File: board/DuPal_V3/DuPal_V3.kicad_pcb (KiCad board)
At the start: 2 copper layers, 116.8 x 73.7 mm, 132 parts, among them J1 ZIF Socket, J2 Debug Header, J3 Extra, J4 Conn_01x21_Pin, J5 Conn_01x21_Pin, K1 G6K-2, Q1 2N3904, SW1 RESET, U1 Pico, U10 74HCT166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

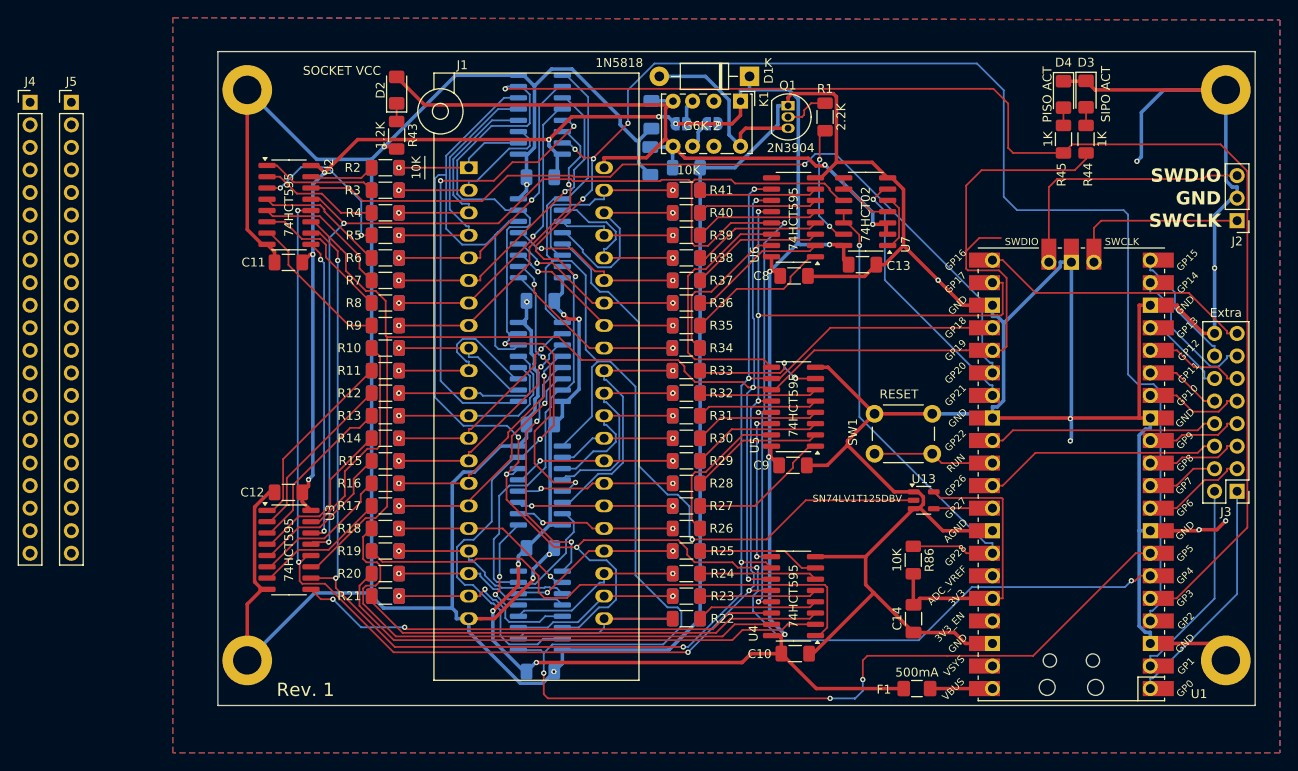
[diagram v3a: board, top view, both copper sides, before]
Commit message: Add pinheaders to rev. 1 V3 board
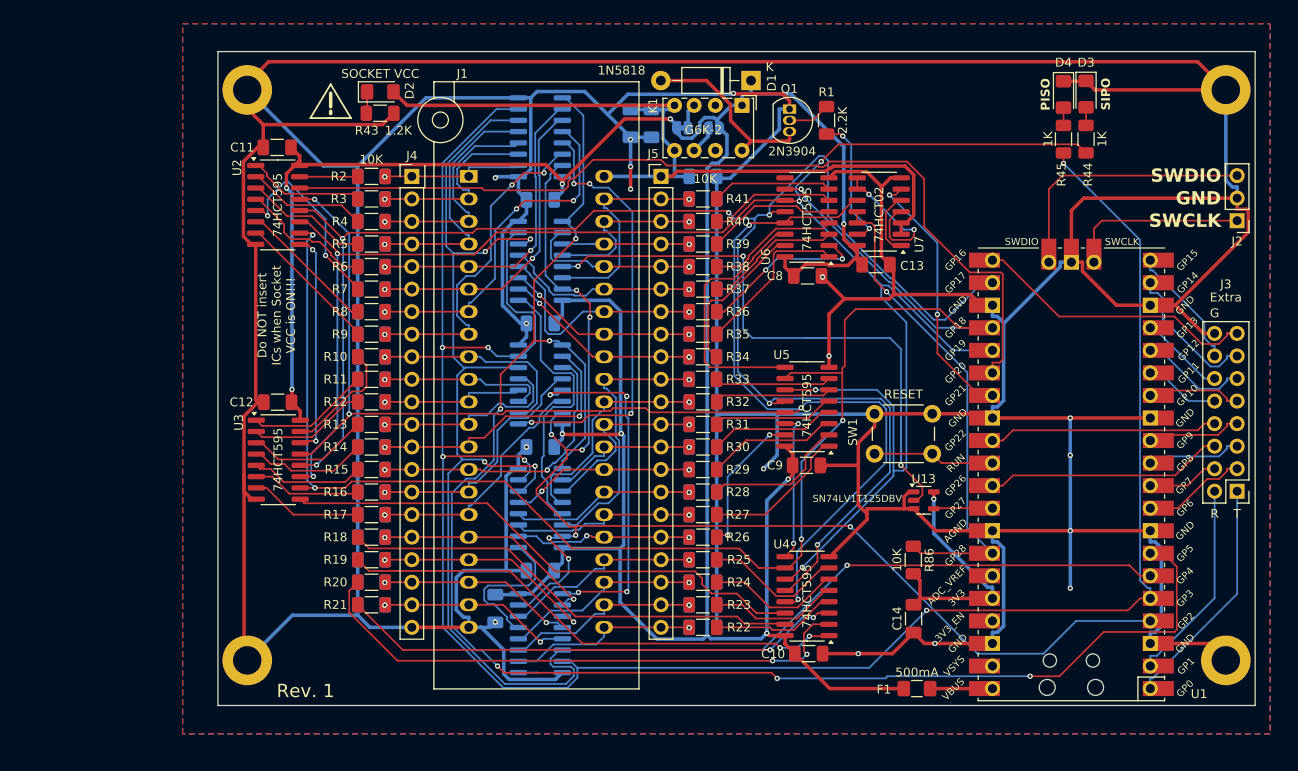
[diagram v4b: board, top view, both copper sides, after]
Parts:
- D3: value SIPO ACT -> SIPO
- D4: value PISO ACT -> PISO
- JP1: footprint Jumper:SolderJumper-2_P1.3mm_Open_RoundedPad1.0x1.5mm -> Jumper:SolderJumper-2_P1.3mm_Bridged_RoundedPad1.0x1.5mm
- moved J5 66.9 mm to (143.9, 54.7)
- moved J4 43.8 mm to (115.8, 54.7)
- moved C11 13.0 mm to (100.6, 51.4)
- moved C12 10.2 mm to (100.7, 80.1)
- moved U3 10.2 mm to (100.8, 86.6)
- moved C7 8.74 mm to (125.2, 103.4), turned to -90 degrees
- moved C1 4.78 mm to (140.5, 48.7)
- moved R43 3.10 mm to (112.2, 47.6), turned to 0 degrees
- moved C3 2.54 mm to (130.3, 99.1), turned to 180 degrees
- moved C4 2.54 mm to (130.3, 85.2)
- moved C5 2.54 mm to (130.3, 71.3)
- moved C6 2.54 mm to (130.3, 57.3)
- moved U12 2.54 mm to (130.3, 64.2)
- moved U8 2.54 mm to (130.3, 50.3)
- moved U10 2.54 mm to (130.3, 106.2)
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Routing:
- net GND: track 708.0 -> 871.3 mm, vias 13 -> 17
- net /PISO_SH: track 209.7 -> 144.6 mm, vias 5 -> 8
- net VCC: track 289.2 -> 326.7 mm, vias 16 -> 9
- net Net-(U10-Ds): track 28.5 -> 40.1 mm, vias 2 -> 4
- net Net-(U3-QA): track 24.4 -> 13.3 mm
- net /SIPO_RCLK: track 183.0 -> 193.0 mm, vias 7 -> 6
- net Net-(U7-Pad4): track 7.27 -> 17.0 mm, vias 0 -> 2
- net Net-(U2-QH'): track 34.5 -> 25.3 mm
- net /~{PISO_CLR}: track 196.5 -> 187.6 mm, vias 3 -> 6
- net /PISO_SER: track 67.6 -> 75.8 mm, vias 1 -> 3
- net /ZIF_9: track 16.0 -> 24.1 mm
- net /SIPO_SER: track 94.1 -> 102.1 mm, vias 1 -> 0
- net /SWITCHED_VCC: track 84.4 -> 92.2 mm, vias 2 -> 0
- net Net-(U4-QA): track 59.9 -> 52.2 mm
- net /ZIF_13: track 24.6 -> 32.1 mm
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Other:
- board text added: "Do NOT insert ICs when Socket VCC is ON!!!"
- board text added: "G"
- board text added: "R"
- board text added: "T"
